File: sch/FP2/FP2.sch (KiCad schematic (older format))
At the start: 13 parts, among them J1 DMX OUT, J2 module_connector, U1 SP485E

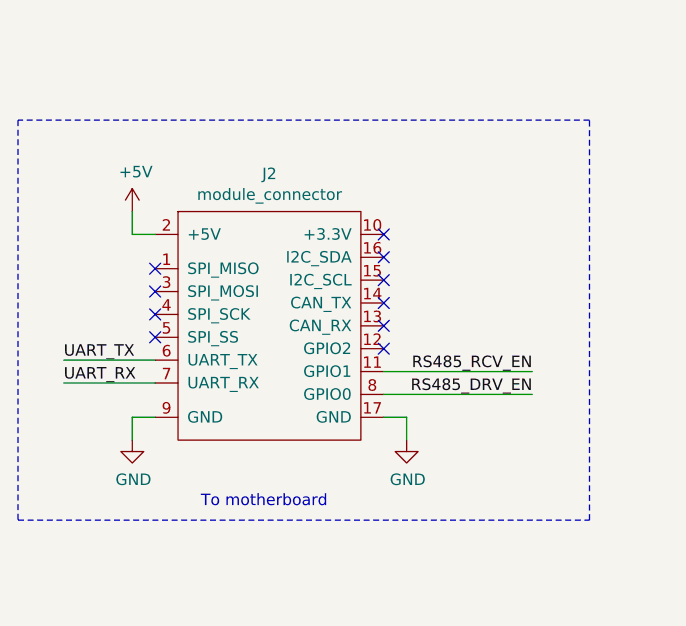
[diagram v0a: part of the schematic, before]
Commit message: Completed BOMs and changed module connector name to 'Faraday_module'
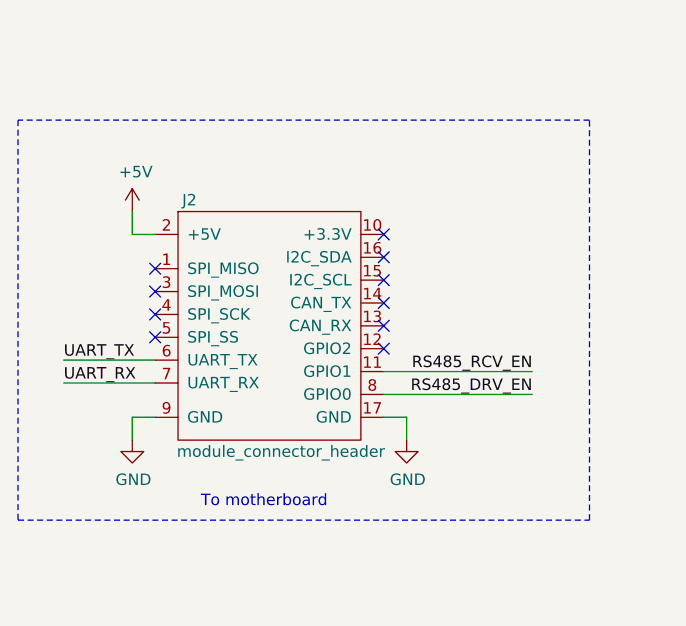
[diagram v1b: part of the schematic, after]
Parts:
- removed J2: module_connector, project_parts:Faraday_module, symbol faraday:module_connector
- added J2: module_connector_header, project_parts:Faraday_module, symbol faraday:module_connector_header
- C1: Manufacturer (none) -> Samsung Electro-mechanics
- C2: Manufacturer (none) -> Murata
- D1: Manufacturer (none) -> Littelfuse; Order Number (none) -> SMBJ43CALFCT-ND; Supplier (none) -> Digikey
- D2: Order Number (none) -> SMBJ43CALFCT-ND; Supplier (none) -> Digikey
- J1: Description (none) -> TERMINAL BLOCK 5.08MM 3POS PCB
- R1, R5, R6: Description 10k 5% 0805 -> RES SMD 10K OHM 1% 1/8W 0805
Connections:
- net +5V: now also J2.2 (+5V)
- net GND: now also J2.17 (GND), J2.9 (GND)
- net RS485_DRV_EN: now also J2.8 (GPIO0)
- net RS485_RCV_EN: now also J2.11 (GPIO1)
- net UART_RX: now also J2.7 (UART_RX)
- net UART_TX: now also J2.6 (UART_TX)
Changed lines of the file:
@@
 F 6 "On Shore Technology" H 9250 3700 50  0001 C CNN "Manufacturer"
 F 7 "OSTYC032150" H 9250 3700 50  0001 C CNN "Part Number"
+F 8 "TERMINAL BLOCK 5.08MM 3POS PCB" H 9250 3700 50  0001 C CNN "Description"
 	1    9250 3700
 	1    0    0    -1
@@
 F 4 "TVS DIODE 43V 69.4V DO214AA" V 7800 4400 50  0001 C CNN "Description"
 F 5 "SMBJ43CA" V 7800 4400 50  0001 C CNN "Part Number"
+F 6 "Digikey" V 7800 4400 50  0001 C CNN "Supplier"
+F 7 "Littelfuse" V 7800 4400 50  0001 C CNN "Manufacturer"
+F 8 "SMBJ43CALFCT-ND" V 7800 4400 50  0001 C CNN "Order Number"
 	1    7800 4400
 	0    1    1    0
@@
 F 2 "Resistor_SMD:R_0805_2012Metric" V 5280 3250 50  0001 C CNN
 F 3 "http://www.yageo.com/documents/recent/PYu-RC_Group_51_RoHS_L_9.pdf" H 5350 3250 50  0001 C CNN
-F 4 "10k 5% 0805" V 5350 3250 50  0001 C CNN "Description"
+F 4 "RES SMD 10K OHM 1% 1/8W 0805" V 5350 3250 50  0001 C CNN "Description"
 F 5 "Yageo" H 5350 3250 50  0001 C CNN "Manufacturer"
 F 6 "RC0805FR-0710KL" H 5350 3250 50  0001 C CNN "Part Number"
@@
 Wire Wire Line
 	3350 4100 2700 4100
-$Comp
-L faraday:module_connector J2
-U 1 1 5BAE257F
-P 2300 3800
-F 0 "J2" H 2200 4465 50  0000 C CNN
-F 1 "module_connector" H 2200 4374 50  0000 C CNN
-F 2 "project_parts:Faraday_module" H 1950 3850 50  0001 C CNN
-F 3 "" H 1950 3850 50  0001 C CNN
-	1    2300 3800
-	1    0    0    -1
-$EndComp
 $Comp
 L power:+5V #PWR0107
@@
 F 1 "100nF 50V" H 7465 2405 50  0000 L CNN
 F 2 "Resistor_SMD:R_0805_2012Metric" H 7388 2300 50  0001 C CNN
-F 3 "~" H 7350 2450 50  0001 C CNN
+F 3 "https://psearch.en.murata.com/capacitor/product/GCM21BR71H104KA37%23.pdf" H 7350 2450 50  0001 C CNN
 F 4 "CAP CER 0.1UF 50V X7R 0805" H 7350 2450 50  0001 C CNN "Description"
 F 5 "GCM21BR71H104KA37K" H 7350 2450 50  0001 C CNN "Part Number"
 F 6 "490-8049-1-ND" H 7350 2450 50  0001 C CNN "Order Number"
 F 7 "Digikey" H 7350 2450 50  0001 C CNN "Supplier"
+F 8 "Murata" H 7350 2450 50  0001 C CNN "Manufacturer"
 	1    7350 2450
 	1    0    0    -1
-$EndComp
-$Comp
-L Device:D_TVS_ALT D2
-U 1 1 5BB334EE
-P 8000 4400
-F 0 "D2" V 7950 4500 50  0000 L CNN
-F 1 "43V 600W" V 8050 4500 50  0000 L CNN
-F 2 "project_parts:D_SMB_NP" H 8000 4400 50  0001 C CNN
-F 3 "http://www.littelfuse.com/~/media/electronics/datasheets/tvs_diodes/littelfuse_tvs_diode_smbj_datasheet.pdf.pdf" H 8000 4400 50  0001 C CNN
-F 4 "TVS DIODE 43V 69.4V DO214AA" V 8000 4400 50  0001 C CNN "Description"
-F 5 "SMBJ43CA" V 8000 4400 50  0001 C CNN "Part Number"
-F 6 "Littelfuse" V 8000 4400 50  0001 C CNN "Manufacturer"
-	1    8000 4400
-	0    1    1    0
 $EndComp
 $Comp
@@
 F 2 "Resistor_SMD:R_0805_2012Metric" V 5480 4050 50  0001 C CNN
 F 3 "http://www.yageo.com/documents/recent/PYu-RC_Group_51_RoHS_L_9.pdf" H 5550 4050 50  0001 C CNN
-F 4 "10k 5% 0805" V 5550 4050 50  0001 C CNN "Description"
+F 4 "RES SMD 10K OHM 1% 1/8W 0805" V 5550 4050 50  0001 C CNN "Description"
 F 5 "Yageo" H 5550 4050 50  0001 C CNN "Manufacturer"
 F 6 "RC0805FR-0710KL" H 5550 4050 50  0001 C CNN "Part Number"
@@
 F 2 "Resistor_SMD:R_0805_2012Metric" V 5280 4050 50  0001 C CNN
 F 3 "http://www.yageo.com/documents/recent/PYu-RC_Group_51_RoHS_L_9.pdf" H 5350 4050 50  0001 C CNN
-F 4 "10k 5% 0805" V 5350 4050 50  0001 C CNN "Description"
+F 4 "RES SMD 10K OHM 1% 1/8W 0805" V 5350 4050 50  0001 C CNN "Description"
 F 5 "Yageo" H 5350 4050 50  0001 C CNN "Manufacturer"
 F 6 "RC0805FR-0710KL" H 5350 4050 50  0001 C CNN "Part Number"
@@
 F 1 "10uF 10V" H 6550 2400 50  0000 L CNN
 F 2 "Resistor_SMD:R_0805_2012Metric" H 7088 2300 50  0001 C CNN
-F 3 "~" H 7050 2450 50  0001 C CNN
+F 3 "https://media.digikey.com/pdf/Data%20Sheets/Samsung%20PDFs/CL_Series_MLCC_ds.pdf" H 7050 2450 50  0001 C CNN
 F 4 "CAP CER 10UF 10V X5R 0805" H 7050 2450 50  0001 C CNN "Description"
 F 5 "CL21A106KPCLQNC" H 7050 2450 50  0001 C CNN "Part Number"
 F 6 "1276-2402-1-ND" H 7050 2450 50  0001 C CNN "Order Number"
 F 7 "Digikey" H 7050 2450 50  0001 C CNN "Supplier"
+F 8 "Samsung Electro-mechanics" H 7050 2450 50  0001 C CNN "Manufacturer"
 	1    7050 2450
 	1    0    0    -1
 $EndComp
+$Comp
+L Device:D_TVS_ALT D2
+U 1 1 5BD26721
+P 8000 4400
+F 0 "D2" V 7950 4500 50  0000 L CNN
+F 1 "43V 600W" V 8050 4500 50  0000 L CNN
+F 2 "project_parts:D_SMB_NP" H 8000 4400 50  0001 C CNN
+F 3 "http://www.littelfuse.com/~/media/electronics/datasheets/tvs_diodes/littelfuse_tvs_diode_smbj_datasheet.pdf.pdf" H 8000 4400 50  0001 C CNN
+F 4 "TVS DIODE 43V 69.4V DO214AA" V 8000 4400 50  0001 C CNN "Description"
+F 5 "SMBJ43CA" V 8000 4400 50  0001 C CNN "Part Number"
+F 6 "Digikey" V 8000 4400 50  0001 C CNN "Supplier"
+F 7 "Littelfuse" V 8000 4400 50  0001 C CNN "Manufacturer"
+F 8 "SMBJ43CALFCT-ND" V 8000 4400 50  0001 C CNN "Order Number"
+	1    8000 4400
+	0    1    1    0
+$EndComp
+$Comp
+L faraday:module_connector_header J2
+U 1 1 5BCD483D
+P 2200 3800
+F 0 "J2" H 1850 4350 50  0000 C CNN
+F 1 "module_connector_header" H 2250 3250 50  0000 C CNN
+F 2 "project_parts:Faraday_module" H 2300 3100 50  0001 C CNN
+F 3 "https://cdn.amphenol-icc.com/media/wysiwyg/files/drawing/68000.pdf" H 2300 3100 50  0001 C CNN
+F 4 "CONN HEADER MALE 18POS .1\"" H 1950 4450 50  0001 C CNN "Description"
+F 5 "Amphenol FCI" H 2200 3800 50  0001 C CNN "Manufacturer"
+F 6 "68001-418HLF" H 2200 3800 50  0001 C CNN "Part Number"
+F 7 "609-5513-ND" H 2200 3800 50  0001 C CNN "Order Number"
+F 8 "Digikey" H 2200 3800 50  0001 C CNN "Supplier"
+	1    2200 3800
+	1    0    0    -1
+$EndComp
